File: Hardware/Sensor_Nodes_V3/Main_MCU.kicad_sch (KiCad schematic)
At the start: 12 parts, among them U1 STM32G474RBTx

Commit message: a lot of progress on V3, still need to test if bootloader works
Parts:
- added C28, C29, C30, C31: 100nF, Capacitor_SMD:C_0402_1005Metric, symbol Device:C
- added D5: RED, LED_SMD:LED_0603_1608Metric, symbol Device:LED
- added J6, J7: Conn_01x27_Socket, Connector_PinHeader_2.54mm:PinHeader_1x27_P2.54mm_Vertical, symbol Connector:Conn_01x27_Socket
- added R18: 220, Resistor_SMD:R_0402_1005Metric, symbol Device:R
- added R19, R20, R21, R22, R23, R24, R25, R26, R27, R28: 2k2, Resistor_SMD:R_0402_1005Metric, symbol Device:R
- added U3, U6: MCP2542FDxMF, Package_DFN_QFN:DFN-8-1EP_3x3mm_P0.65mm_EP1.55x2.4mm, symbol Interface_CAN_LIN:MCP2542FDxMF
- C22, C23, C24, C25: footprint (none) -> Capacitor_SMD:C_0402_1005Metric
- L2: footprint (none) -> Inductor_SMD:L_0603_1608Metric
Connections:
- net +3.3V: now also C28.1, C30.1, J6.4 (Pin_4), J7.4 (Pin_4), R19.1, R20.1, R21.1, R22.1, R23.1, R24.1, R25.1, R26.1, R27.1, R28.1, U3.5 (VIO), U6.5 (VIO)
- net GND: now also U1.15 (VSS), U1.27 (VSSA), U1.31 (VSS), U1.47 (VSS), U1.63 (VSS), C28.2, C29.2, C30.2, C31.2, J6.2 (Pin_2), J7.2 (Pin_2), R18.1, U3.2 (VSS), U3.9 (VSS), U6.2 (VSS), U6.9 (VSS)
- net PC2: now reaches U1.10 (PC2)
- net PC2: now also J7.26 (Pin_26)
- net PC3: now reaches U1.11 (PC3)
- net PC3: now also J7.27 (Pin_27)
- net PA0: now reaches U1.12 (PA0)
- net PA0: now also J6.27 (Pin_27)
- net PA1: now reaches U1.13 (PA1)
- net PA1: now also J6.26 (Pin_26)
- net PA2: now reaches U1.14 (PA2)
- net PA2: now also J6.25 (Pin_25)
- net PA3: now reaches U1.17 (PA3)
- net PA3: now also J6.24 (Pin_24)
- net PA4: now reaches U1.18 (PA4)
- net PA4: now also J6.23 (Pin_23)
- net SPI1_SCK: now reaches U1.19 (PA5)
- net SPI1_SCK: now also J6.22 (Pin_22)
- net PC13: now reaches U1.2 (PC13)
- net PC13: now also J7.21 (Pin_21)
- net SPI1_MISO: now reaches U1.20 (PA6)
- net SPI1_MISO: now also J6.20 (Pin_20), R28.2
- net SPI1_MOSI: now reaches U1.21 (PA7)
- net SPI1_MOSI: now also J6.21 (Pin_21)
- net PC4: now reaches U1.22 (PC4)
- net PC4: now also J6.19 (Pin_19)
- net PC5: now reaches U1.23 (PC5)
- net PC5: now also J6.18 (Pin_18)
- net PB0: now reaches U1.24 (PB0)
- net PB0: now also J6.17 (Pin_17)
- net PB1: now reaches U1.25 (PB1)
- net PB1: now also J6.16 (Pin_16)
- net PB2: now reaches U1.26 (PB2)
- net PB2: now also J6.15 (Pin_15)
- net PC14: now reaches U1.3 (PC14)
- net PC14: now also J7.22 (Pin_22)
- net PB10: now reaches U1.30 (PB10)
- net PB10: now also J6.14 (Pin_14)
- net PB11: now reaches U1.33 (PB11)
- net PB11: now also J6.13 (Pin_13)
- net CRXD2: now reaches U1.34 (PB12)
- net CRXD2: now also U6.4 (RXD)
- net CTXD2: now reaches U1.35 (PB13)
- net CTXD2: now also U6.1 (TXD)
- net PB14: now reaches U1.36 (PB14)
- net PB14: now also J6.9 (Pin_9)
- net PB15: now reaches U1.37 (PB15)
- net PB15: now also J6.12 (Pin_12)
- net I2C4_SCL: now reaches U1.38 (PC6)
- net I2C4_SCL: now also J6.7 (Pin_7), R19.2
- net I2C4_SDA: now reaches U1.39 (PC7)
- net I2C4_SDA: now also J6.8 (Pin_8), R20.2
- net PC15: now reaches U1.4 (PC15)
- net PC15: now also J7.23 (Pin_23)
- net I2C3_SCL: now reaches U1.40 (PC8)
- net I2C3_SCL: now also J6.6 (Pin_6), R21.2
- net I2C3_SDA: now reaches U1.41 (PC9)
- net I2C3_SDA: now also J6.5 (Pin_5), R22.2
- net I2C2_SDA: now reaches U1.42 (PA8)
- net I2C2_SDA: now also J7.9 (Pin_9), R24.2
- net I2C2_SCL: now reaches U1.43 (PA9)
- net I2C2_SCL: now also J7.8 (Pin_8), R23.2
- net PA10: now reaches U1.44 (PA10)
- net PA10: now also J7.7 (Pin_7)
- net CRXD3: now reaches U1.45 (PA11)
- net CRXD3: now also U3.4 (RXD)
- net CTXD3: now reaches U1.46 (PA12)
- net CTXD3: now also U3.1 (TXD)
- net T_SWO: now reaches U1.49 (PA13)
- net XTAL_S: now reaches U1.5 (PF0)
- net T_CLK: now reaches U1.50 (PA14)
- net HBEAT: now reaches U1.51 (PA15)
- net HBEAT: now also D5.2 (A)
- net SPI3_SCK: now reaches U1.52 (PC10)
- net SPI3_SCK: now also J7.10 (Pin_10)
- net SPI3_MISO: now reaches U1.53 (PC11)
- net SPI3_MISO: now also J7.11 (Pin_11), R27.2
- net SPI3_MOSI: now reaches U1.54 (PC12)
- net SPI3_MOSI: now also J7.12 (Pin_12)
- net PD2: now reaches U1.55 (PD2)
- net PD2: now also J7.13 (Pin_13)
- net PB3: now reaches U1.56 (PB3)
- net PB3: now also J7.14 (Pin_14)
- net PB4: now reaches U1.57 (PB4)
- net PB4: now also J7.15 (Pin_15)
- net PB5: now reaches U1.58 (PB5)
- net PB5: now also J7.16 (Pin_16)
- net PB6: now reaches U1.59 (PB6)
- net PB6: now also J7.17 (Pin_17)
- net I2C1_SDA: now reaches U1.60 (PB7)
- net I2C1_SDA: now also J7.18 (Pin_18), R26.2
- net I2C1_SCL: now reaches U1.61 (PB8)
- net I2C1_SCL: now also J7.19 (Pin_19), R25.2
- net PB9: now reaches U1.62 (PB9)
- net PB9: now also J7.20 (Pin_20)
- net T_RST: now reaches U1.7 (PG10)
- net PC0: now reaches U1.8 (PC0)
- net PC0: now also J7.24 (Pin_24)
- net PC1: now reaches U1.9 (PC1)
- net PC1: now also J7.25 (Pin_25)
- new net: D5.1 (K), R18.2
- new net +12V: J6.1 (Pin_1), J7.1 (Pin_1)
- new net +5V: C29.1, C31.1, J6.3 (Pin_3), J7.3 (Pin_3), U3.3 (VDD), U6.3 (VDD)
- new net CANH2: J6.10 (Pin_10), U6.7 (CANH)
- new net CANH3: J7.6 (Pin_6), U3.7 (CANH)
- new net CANL2: J6.11 (Pin_11), U6.6 (CANL)
- new net CANL3: J7.5 (Pin_5), U3.6 (CANL)
- no-connect marks 0 -> 3
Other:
- moved on the sheet: C16, C17, C18, C19, C20, C21, C22, C23, C24, C25, L2, U1

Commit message: sync update
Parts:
- removed C20: 100nF, Capacitor_SMD:C_0402_1005Metric, symbol Device:C
- C16, C17, C18, C19, C21, C22, C23, C24, C25, C28, C29, C30, C31: footprint Capacitor_SMD:C_0402_1005Metric -> Capacitor_SMD:C_0603_1608Metric
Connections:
- net +3V3 is gone; now on net +3.3V: C16.1, C17.1, C18.1, C19.1, C21.1
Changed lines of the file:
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@@
 	)
 	(junction
-		(at 240.03 26.67)
-		(diameter 0)
-		(color 0 0 0 0)
-	)
-	(junction
 		(at 250.19 59.69)
 		(diameter 0)
@@
 	)
 	(junction
-		(at 240.03 36.83)
-		(diameter 0)
-		(color 0 0 0 0)
-	)
-	(junction
 		(at 48.26 24.13)
 		(diameter 0)
@@
 	(wire
 		(pts
-			(xy 240.03 26.67) (xy 240.03 27.94)
-		)
-		(stroke
-			(width 0)
-			(type default)
-		)
-	)
-	(wire
-		(pts
 			(xy 68.58 102.87) (xy 73.66 102.87)
 		)
@@
 		)
 	)
-	(wire
-		(pts
-			(xy 240.03 35.56) (xy 240.03 36.83)
-		)
-		(stroke
-			(width 0)
-			(type default)
-		)
-	)
 	(polyline
 		(pts
@@
 	(wire
 		(pts
-			(xy 233.68 26.67) (xy 240.03 26.67)
+			(xy 233.68 26.67) (xy 246.38 26.67)
 		)
 		(stroke
@@
 	(wire
 		(pts
-			(xy 246.38 36.83) (xy 240.03 36.83)
-		)
-		(stroke
-			(width 0)
-			(type default)
-		)
-	)
-	(wire
-		(pts
 			(xy 68.58 59.69) (xy 73.66 59.69)
 		)
@@
 	(wire
 		(pts
-			(xy 246.38 26.67) (xy 240.03 26.67)
-		)
-		(stroke
-			(width 0)
-			(type default)
-		)
-	)
-	(wire
-		(pts
 			(xy 209.55 59.69) (xy 220.98 59.69)
 		)
@@
 	(wire
 		(pts
-			(xy 240.03 36.83) (xy 233.68 36.83)
+			(xy 233.68 36.83) (xy 246.38 36.83)
 		)
 		(stroke
@@
 			)
 		)
-		(property "Footprint" "Capacitor_SMD:C_0402_1005Metric"
+		(property "Footprint" "Capacitor_SMD:C_0603_1608Metric"
 			(at 215.5952 35.56 0)
 			(effects
@@
 			)
 		)
-		(property "Value" "+3V3"
+		(property "Value" "+3.3V"
 			(at 215.011 21.0058 0)
 			(effects
@@
 			)
 		)
-		(property "Footprint" "Capacitor_SMD:C_0402_1005Metric"
+		(property "Footprint" "Capacitor_SMD:C_0603_1608Metric"
 			(at 228.2952 35.56 0)
 			(effects
@@
 			)
 		)
-		(property "Footprint" "Capacitor_SMD:C_0402_1005Metric"
+		(property "Footprint" "Capacitor_SMD:C_0603_1608Metric"
 			(at 210.5152 68.58 0)
 			(effects
@@
 			)
 		)
-		(property "Footprint" "Capacitor_SMD:C_0402_1005Metric"
+		(property "Footprint" "Capacitor_SMD:C_0603_1608Metric"
 			(at 251.1552 67.31 0)
 			(effects
@@
 			)
 		)
-		(property "Footprint" "Capacitor_SMD:C_0402_1005Metric"
+		(property "Footprint" "Capacitor_SMD:C_0603_1608Metric"
 			(at 234.6452 35.56 0)
 			(effects
@@
 			)
 		)
-		(property "Footprint" "Capacitor_SMD:C_0402_1005Metric"
+		(property "Footprint" "Capacitor_SMD:C_0603_1608Metric"
 			(at 200.3552 133.35 0)
 			(effects
@@
 			)
 		)
-		(property "Footprint" "Capacitor_SMD:C_0402_1005Metric"
+		(property "Footprint" "Capacitor_SMD:C_0603_1608Metric"
 			(at 247.3452 35.56 0)
 			(effects
@@
 			)
 		)
-		(property "Footprint" "Capacitor_SMD:C_0402_1005Metric"
+		(property "Footprint" "Capacitor_SMD:C_0603_1608Metric"
 			(at 246.0752 133.35 0)
 			(effects
@@
 			)
 		)
-		(property "Footprint" "Capacitor_SMD:C_0402_1005Metric"
+		(property "Footprint" "Capacitor_SMD:C_0603_1608Metric"
 			(at 221.9452 68.58 0)
 			(effects
@@
 			)
 		)
-		(property "Footprint" "Capacitor_SMD:C_0402_1005Metric"
+		(property "Footprint" "Capacitor_SMD:C_0603_1608Metric"
 			(at 274.0152 133.35 0)
 			(effects
@@
 			)
 		)
-		(property "Footprint" "Capacitor_SMD:C_0402_1005Metric"
+		(property "Footprint" "Capacitor_SMD:C_0603_1608Metric"
 			(at 221.9452 35.56 0)
 			(effects
@@
 	)
 	(symbol
-		(lib_id "Device:C")
-		(at 240.03 31.75 0)
-		(unit 1)
-		(exclude_from_sim no)
-		(in_bom yes)
-		(on_board yes)
-		(dnp no)
-		(property "Reference" "C20"
-			(at 240.03 29.21 0)
-			(effects
-				(font
-					(size 1.27 1.27)
-				)
-				(justify left)
-			)
-		)
-		(property "Value" "100nF"
-			(at 240.03 34.29 0)
-			(effects
-				(font
-					(size 1.27 1.27)
-				)
-				(justify left)
-			)
-		)
-		(property "Footprint" "Capacitor_SMD:C_0402_1005Metric"
-			(at 240.9952 35.56 0)
-			(effects
-				(font
-					(size 1.27 1.27)
-				)
-				(hide yes)
-			)
-		)
-		(property "Datasheet" "~"
-			(at 240.03 31.75 0)
-			(effects
-				(font
-					(size 1.27 1.27)
-				)
-				(hide yes)
-			)
-		)
-		(property "Description" "Unpolarized capacitor"
-			(at 240.03 31.75 0)
-			(effects
-				(font
-					(size 1.27 1.27)
-				)
-				(hide yes)
-			)
-		)
-		(property "LCSC" "C1525"
-			(at 240.03 31.75 0)
-			(effects
-				(font
-					(size 1.27 1.27)
-				)
-				(hide yes)
-			)
-		)
-		(pin "1"
-		)
-		(pin "2"
-		)
-		(instances
-			(project "gr25_nodes"
-				(path "/7b4e8e38-4440-451f-8c12-a5c49d6e3525/466e2466-e768-4b2c-901e-6531e50d4122"
-					(reference "C20")
-					(unit 1)
-				)
-			)
-		)
-	)
-	(symbol
 		(lib_id "Device:L")
 		(at 204.47 59.69 90)
@@
 			)
 		)
-		(property "Footprint" "Capacitor_SMD:C_0402_1005Metric"
+		(property "Footprint" "Capacitor_SMD:C_0603_1608Metric"
 			(at 238.4552 67.31 0)
 			(effects
@@
 			)
 		)
-		(property "Footprint" "Capacitor_SMD:C_0402_1005Metric"
+		(property "Footprint" "Capacitor_SMD:C_0603_1608Metric"
 			(at 228.2952 133.35 0)
 			(effects

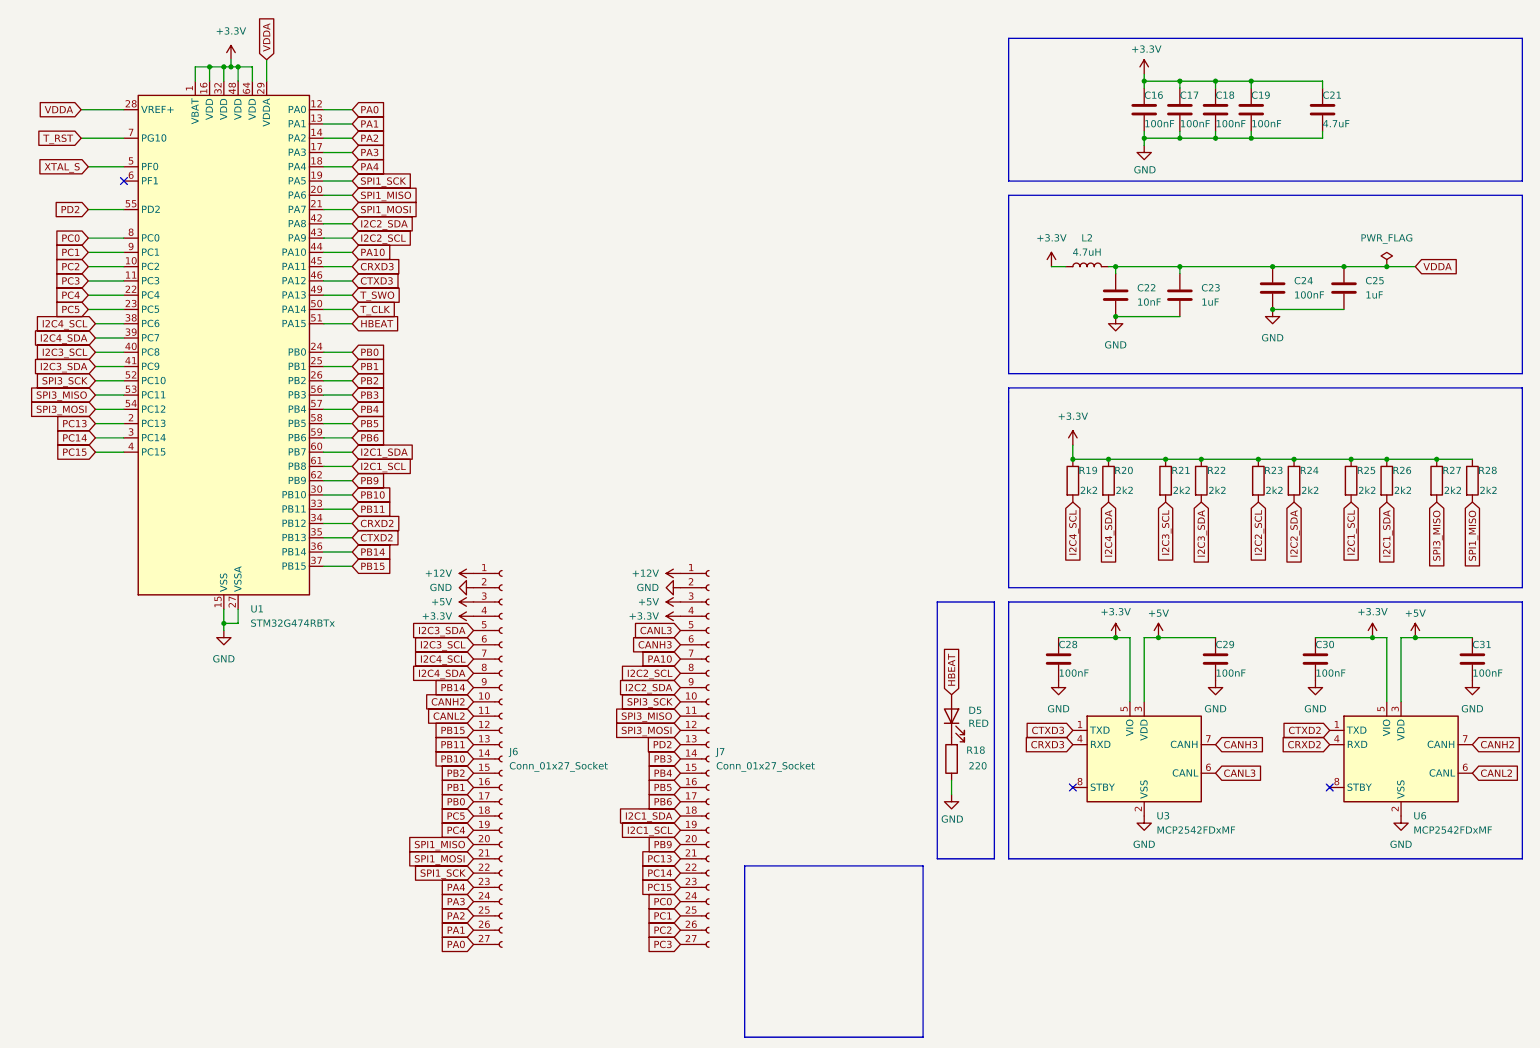
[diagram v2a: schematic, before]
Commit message: finished v3, need to fix drc silkscreens
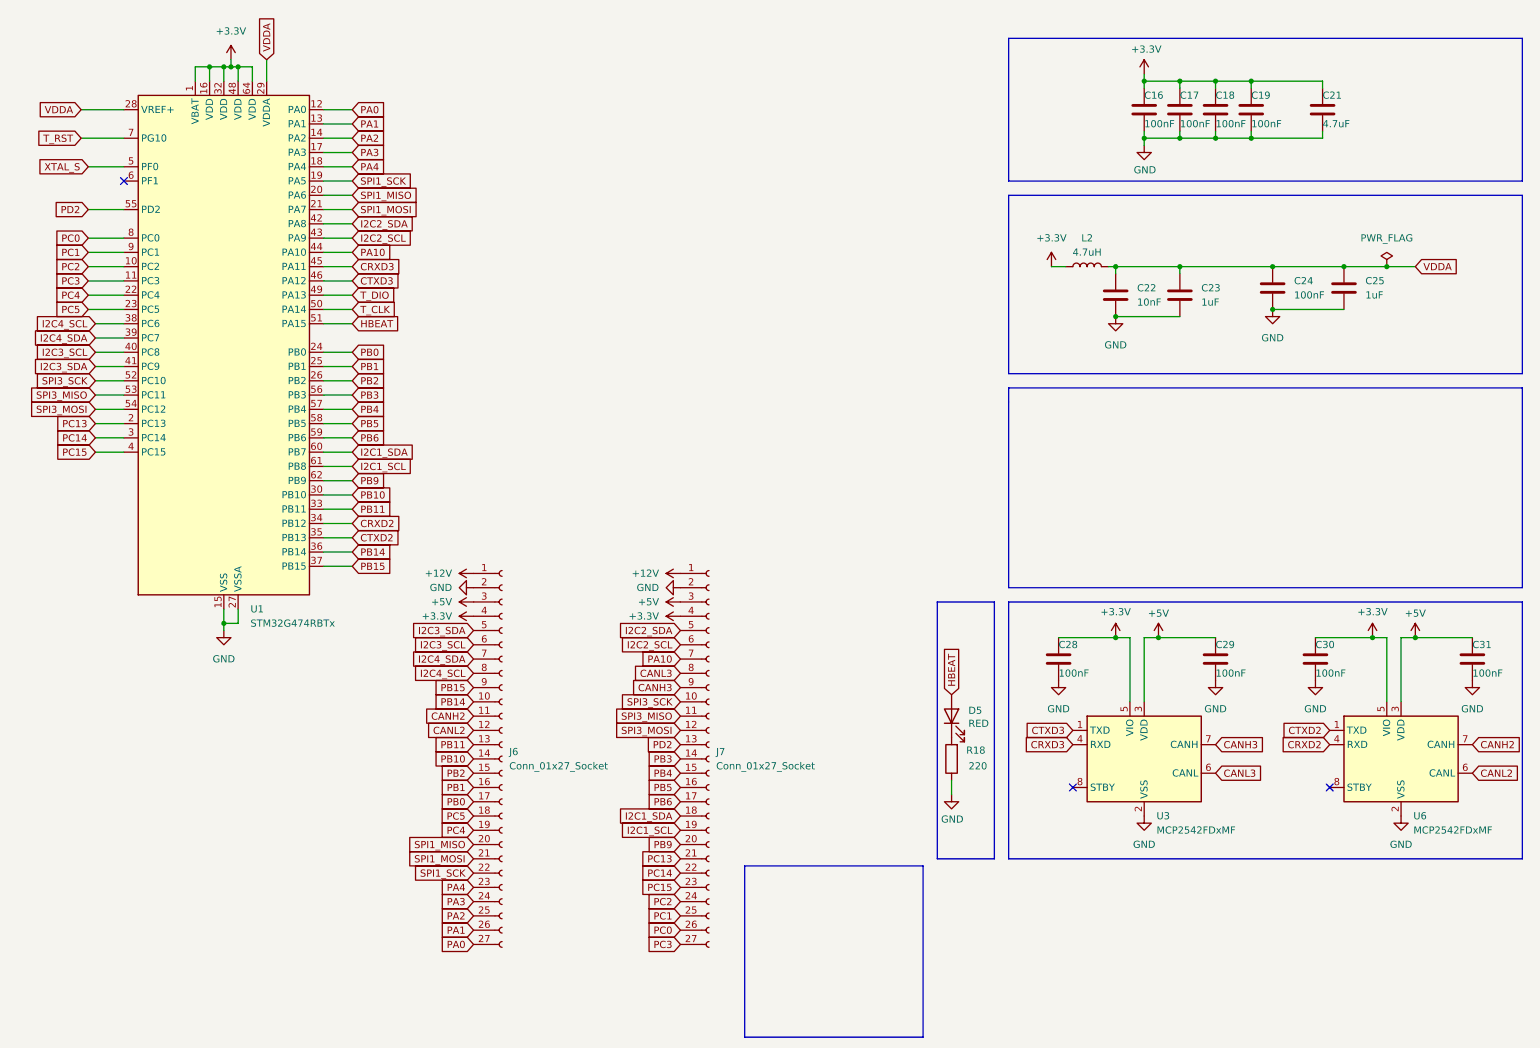
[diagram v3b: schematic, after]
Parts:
- removed R19, R20, R21, R22, R23, R24, R25, R26, R27, R28: 2k2, Resistor_SMD:R_0402_1005Metric, symbol Device:R
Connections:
- net CANH2: now also J6.11 (Pin_11); no longer J6.10 (Pin_10)
- net CANH3: now also J7.9 (Pin_9); no longer J7.6 (Pin_6)
- net CANL2: now also J6.12 (Pin_12); no longer J6.11 (Pin_11)
- net CANL3: now also J7.8 (Pin_8); no longer J7.5 (Pin_5)
- net I2C2_SCL: now also J7.6 (Pin_6); no longer J7.8 (Pin_8)
- net I2C2_SDA: now also J7.5 (Pin_5); no longer J7.9 (Pin_9)
- net I2C4_SCL: now also J6.8 (Pin_8); no longer J6.7 (Pin_7)
- net I2C4_SDA: now also J6.7 (Pin_7); no longer J6.8 (Pin_8)
- net PB14: now also J6.10 (Pin_10); no longer J6.9 (Pin_9)
- net PB15: now also J6.9 (Pin_9); no longer J6.12 (Pin_12)
- net PC0: now also J7.26 (Pin_26); no longer J7.24 (Pin_24)
- net PC2: now also J7.24 (Pin_24); no longer J7.26 (Pin_26)
- net T_SWO renamed T_DIO
